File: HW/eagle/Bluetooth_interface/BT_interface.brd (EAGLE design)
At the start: 40.5 x 30 mm, 46 parts, among them IC3 FT232RL, IC5 UA78M05DCY

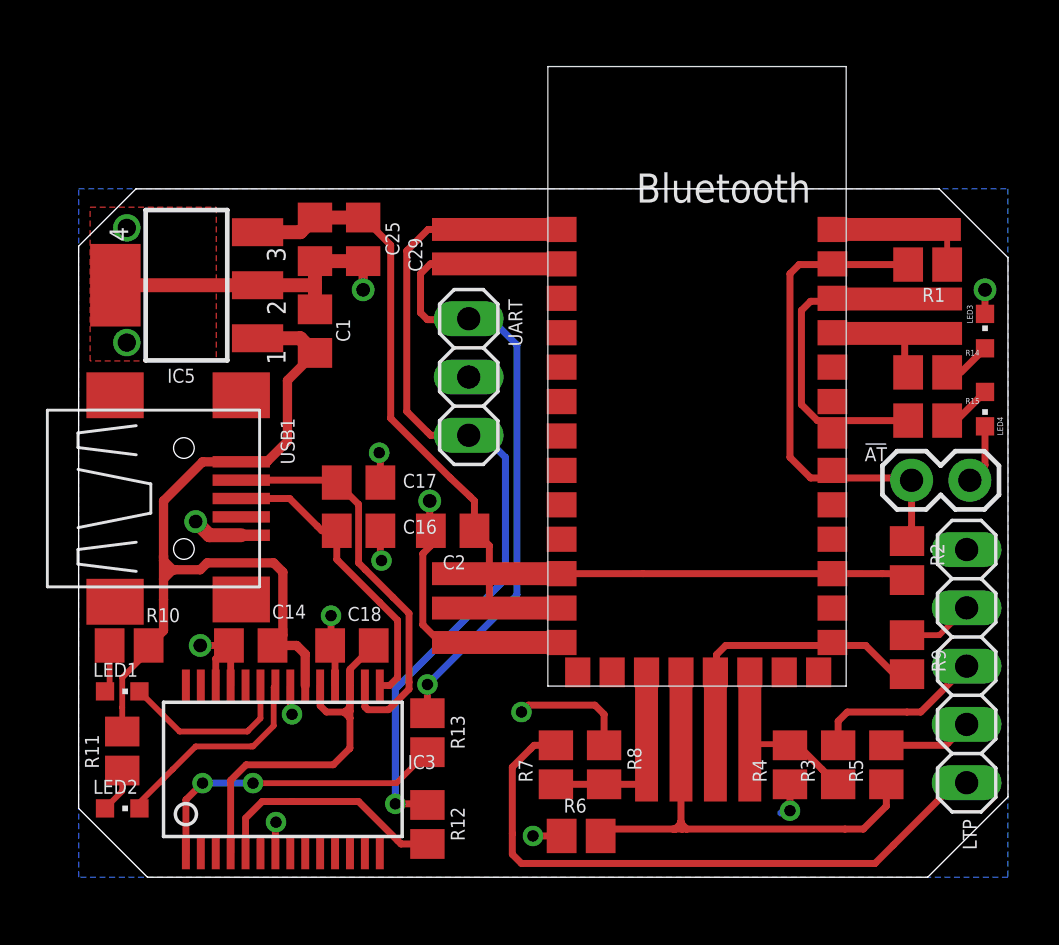
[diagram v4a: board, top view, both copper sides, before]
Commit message: Reference Designators resized rearranged
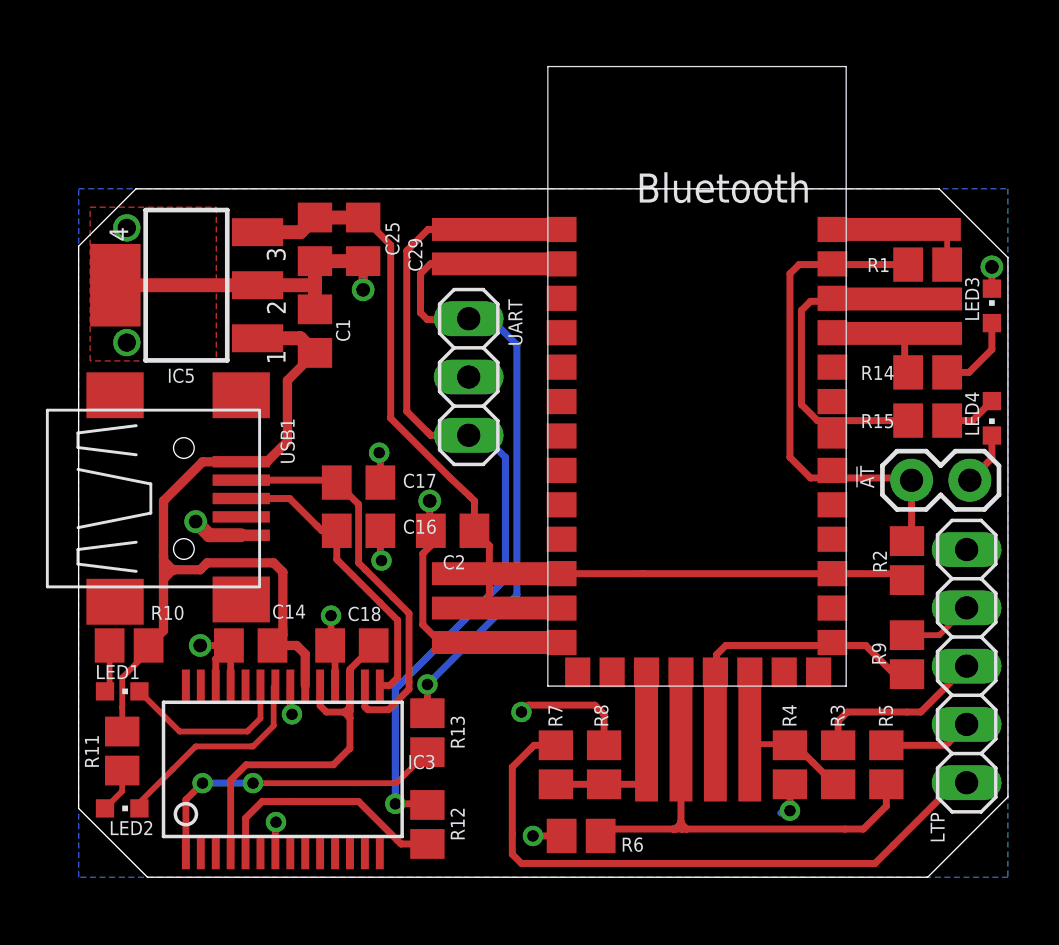
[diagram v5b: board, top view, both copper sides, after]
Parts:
- moved LED3 1.14 mm to (39.8, 24.9)
- moved LED4 0.50 mm to (39.8, 20.0)
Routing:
- net N$12: track 2.08 -> 3.51 mm

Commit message: bluetooth module footprint removed and replaced with dummy drawing
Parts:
- removed U$1: BLUETOOTH, daGloane:BLUETOOTH
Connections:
- removed net 3.3V: U$1.P$12
- removed net GND1: U$1.P$14
- removed net GND2: U$1.P$21
- removed net GND3: U$1.P$22
- net GND: no longer U$1.P$13
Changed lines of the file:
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@@
 <attribute name="VALUE" x="6.0208" y="23.26" size="0.6096" layer="27" rot="R90"/>
 </element>
-<element name="U$1" library="daGloane" package="BLUETOOTH" value="BLUETOOTH" x="26.8" y="23.9" smashed="yes"/>
 <element name="C1" library="rcl" package="C0805" value="10µ" x="10.3" y="23.8" smashed="yes" rot="R90">
 <attribute name="NAME" x="11.83" y="23.33" size="0.6096" layer="25" font="vector" rot="R90"/>
@@
 <wire x1="15" y1="14.1" x2="15.35" y2="14.45" width="0.3048" layer="1"/>
 <wire x1="15.35" y1="14.45" x2="15.35" y2="15.1" width="0.3048" layer="1"/>
-<contactref element="U$1" pad="P$13"/>
 <wire x1="19.8" y1="1.8" x2="21.05" y2="1.8" width="0.3048" layer="1"/>
 <contactref element="!AT" pad="2"/>
@@
 <via x="39.8" y="26.6" extent="1-16" drill="0.6"/>
 <wire x1="21.05" y1="1.8" x2="21.1" y2="1.8" width="0.3048" layer="1"/>
-<wire x1="22.5" y1="7.5" x2="21.05" y2="10.23" width="0" layer="19" extent="1-1"/>
 </signal>
 <signal name="VDDIO">
@@
 <wire x1="19.1" y1="12.3" x2="19.1" y2="12.8" width="0.3048" layer="16"/>
 </signal>
-<signal name="GND1">
-<contactref element="U$1" pad="P$14"/>
-</signal>
-<signal name="GND2">
-<contactref element="U$1" pad="P$21"/>
-</signal>
-<signal name="GND3">
-<contactref element="U$1" pad="P$22"/>
-</signal>
 <signal name="N$12">
 <contactref element="R14" pad="1"/>
@@
 <wire x1="36.15" y1="19.9" x2="32.2" y2="19.9" width="0.3048" layer="1"/>
 </signal>
-<signal name="3.3V">
-<contactref element="U$1" pad="P$12"/>
-</signal>
 </signals>
